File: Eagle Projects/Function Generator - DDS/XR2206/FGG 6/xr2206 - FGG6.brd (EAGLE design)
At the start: 100.3 x 74.6 mm, 70 parts, among them IC1 TL081N, IC2 XR2206CP-F, IC3 TL081N, IC4 74HC14N, IC5 78L05, IC6 7905, J1 Clock-Not, J2-V+ V+, J3-V- V-, J4 Clock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

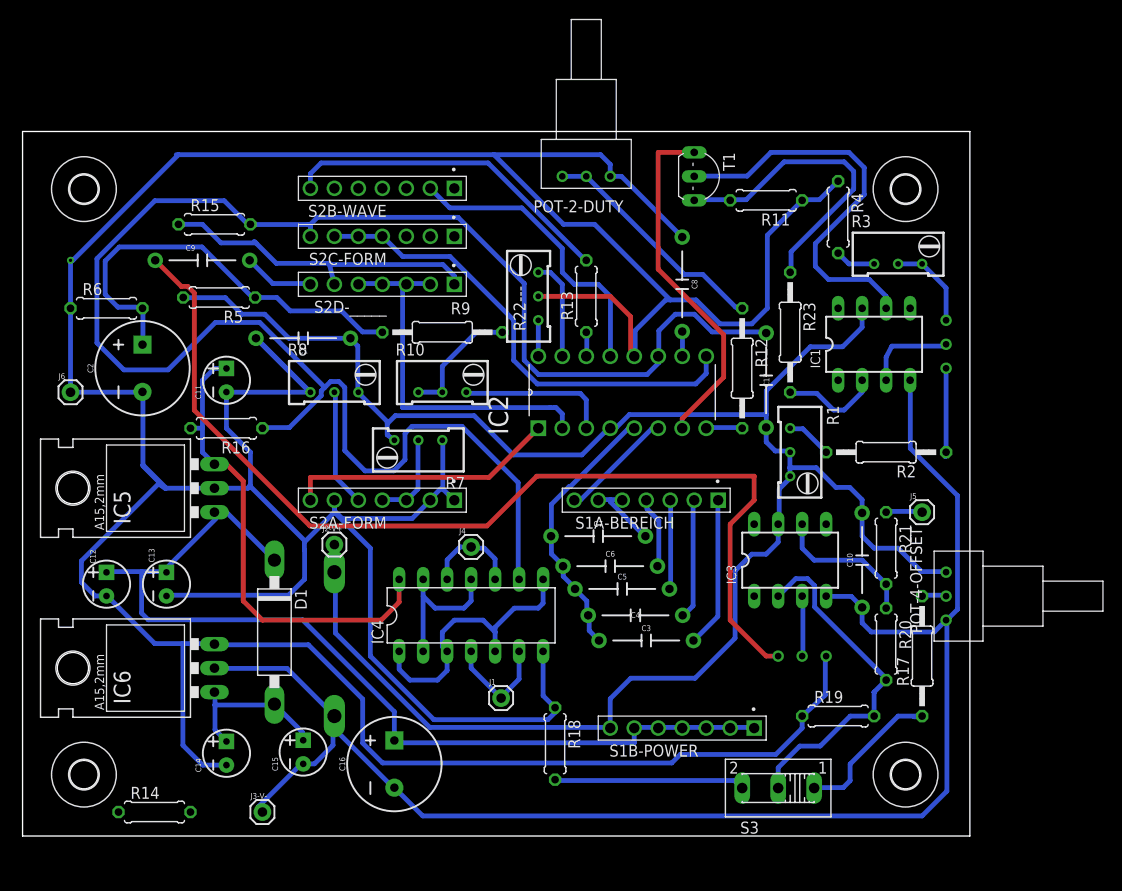
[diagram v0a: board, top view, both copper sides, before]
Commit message: Adding Coil winder
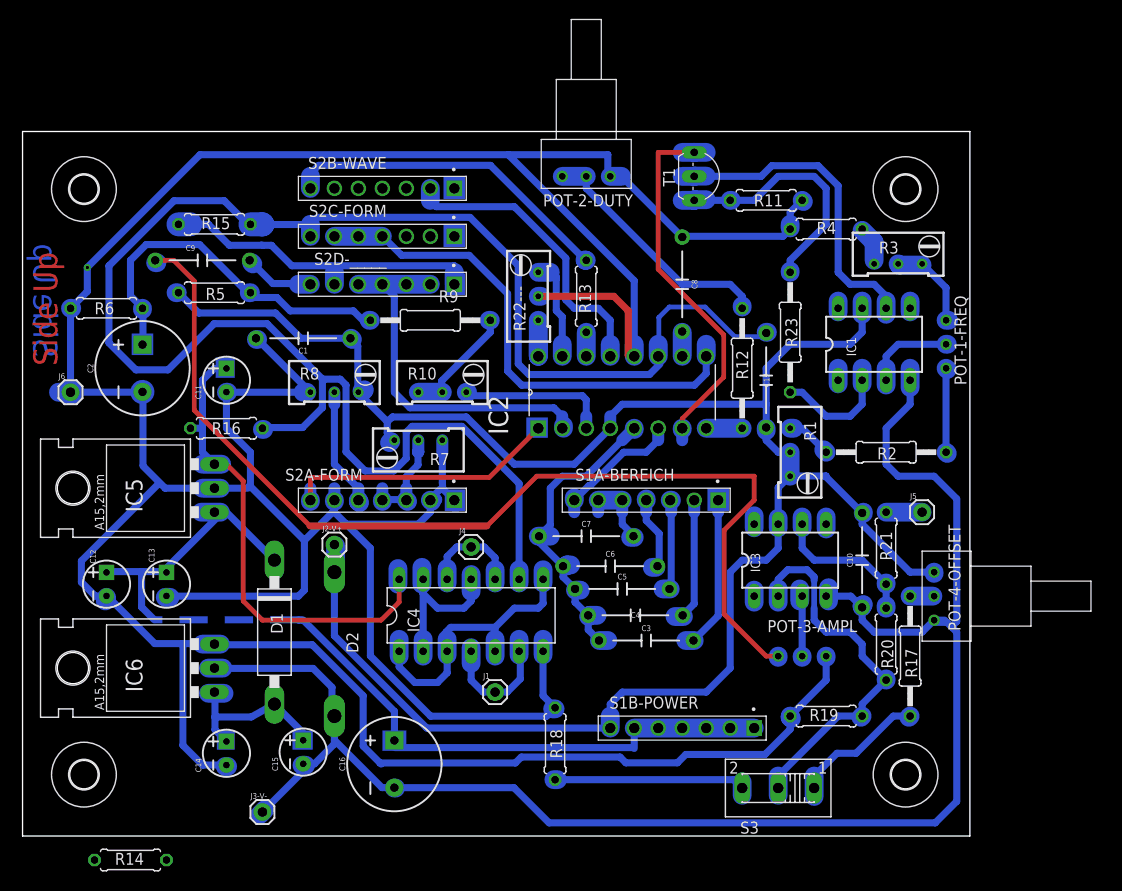
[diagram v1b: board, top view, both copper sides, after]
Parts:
- moved R14 5.68 mm to (11.4, -2.54)
- moved R9 1.80 mm to (43.2, 54.6)
- moved R4 1.80 mm to (85.1, 64.3), turned to 0 degrees
- moved POT-4-OFFSET 1.27 mm to (96.5, 25.4)
- moved C7 1.27 mm to (59.7, 31.8)
- moved R17 1.27 mm to (94.0, 19.1)
- moved R19 1.27 mm to (85.1, 12.7)
- moved J1 0.90 mm to (50.0, 15.2)
- moved R5 0.72 mm to (20.3, 57.5)
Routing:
- net -18V: track 162.2 -> 177.2 mm
- net N$5: track 102.6 -> 116.7 mm
- net GND: track 463.0 -> 449.5 mm
- net +18V: track 208.7 -> 220.7 mm
- net N$31: track 50.6 -> 59.4 mm
- net N$33: track 39.8 -> 48.1 mm
- net N$44: track 37.0 -> 43.5 mm
- net N$12: track 46.0 -> 40.0 mm
- net N$32: track 187.1 -> 192.9 mm
- net N$34: track 30.0 -> 35.4 mm
- net N$8: track 42.4 -> 37.1 mm
- net N$35: track 15.8 -> 21.0 mm
- net N$11: track 37.7 -> 41.6 mm
- net N$10: track 32.6 -> 28.7 mm
- net N$48: track 3.81 -> 7.62 mm
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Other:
- board text added: "Side Up"
